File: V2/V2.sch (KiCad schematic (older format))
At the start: 184 parts, among them U1 Elite-C

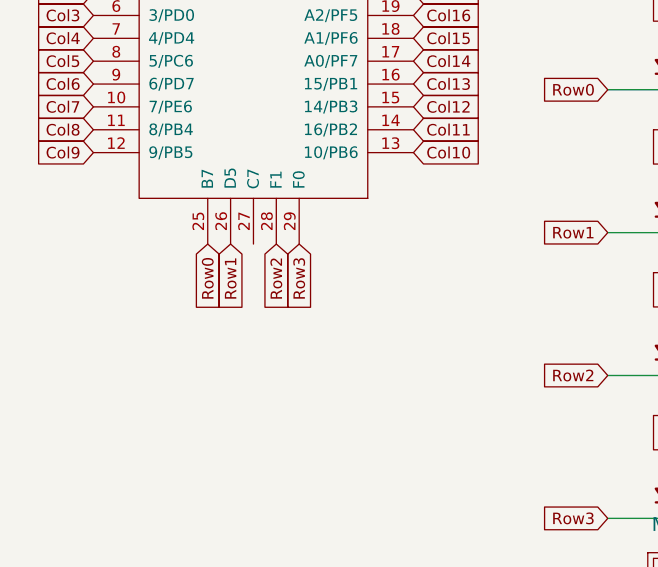
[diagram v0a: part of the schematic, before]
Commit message: Switched to LED
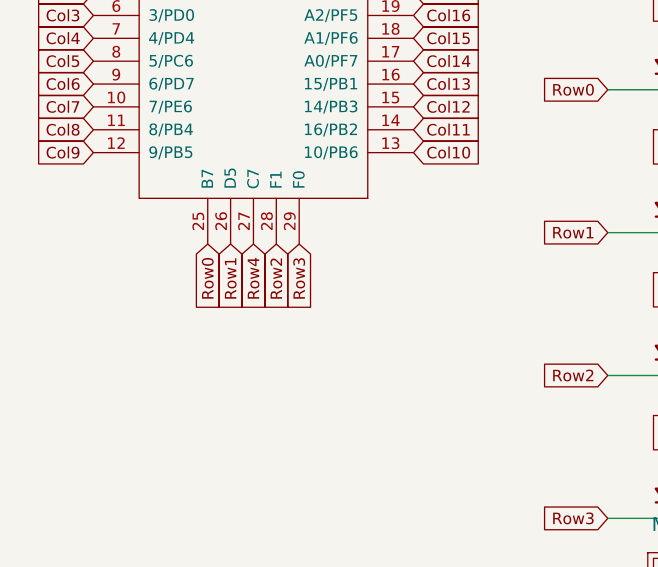
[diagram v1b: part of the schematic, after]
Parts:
- MX1, MX10, MX11, MX12, MX13, MX14, MX15, MX16, MX2, MX20, MX25, MX26, MX27, MX28, MX29, MX3, MX30, MX31, MX32, MX33, MX35, MX36, MX37, MX38, MX39, MX4, MX40, MX41, MX42, MX44, MX45, MX46, MX47, MX48, MX49, MX5, MX50, MX51, MX52, MX53, MX54, MX55, MX56, MX58, MX59, MX6, MX60, MX61, MX63, MX64, MX65, MX66, MX68, MX69, MX7, MX70, MX72, MX73, MX74, MX75, MX77, MX78, MX79, MX8, MX81, MX85, MX86, MX87, MX88, MX89, MX9, MX90, MX91: footprint MX_Alps_Hybrid:MXOnly-1U-Hotswap -> MX_Alps_Hybrid:MXOnly-1U
- MX17, MX18, MX82: footprint MX_Alps_Hybrid:MXOnly-2U-Hotswap -> MX_Alps_Hybrid:MXOnly-2U
- MX19, MX24, MX34, MX62, MX67, MX71, MX76: footprint MX_Alps_Hybrid:MXOnly-1.25U-Hotswap -> MX_Alps_Hybrid:MXOnly-1.25U
- MX21, MX83: footprint MX_Alps_Hybrid:MXOnly-1.5U-Hotswap -> MX_Alps_Hybrid:MXOnly-1.5U
- MX22, MX80: footprint MX_Alps_Hybrid:MXOnly-1.75U-Hotswap -> MX_Alps_Hybrid:MXOnly-1.75U
- MX23, MX84: footprint MX_Alps_Hybrid:MXOnly-2.25U-Hotswap -> MX_Alps_Hybrid:MXOnly-2.25U
- MX43: footprint MX_Alps_Hybrid:MXOnly-2.25U-Hotswap-ReversedStabilizers -> MX_Alps_Hybrid:MXOnly-2.25U-ReversedStabilizers
- MX57: footprint MX_Alps_Hybrid:MXOnly-2.75U-Hotswap-ReversedStabilizers -> MX_Alps_Hybrid:MXOnly-2.75U
- MX92: footprint MX_Alps_Hybrid:MXOnly-2U-Hotswap-ReversedStabilizers -> MX_Alps_Hybrid:MXOnly-2U-ReversedStabilizers
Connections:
- net Row4: now also U1.27 (C7)

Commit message: Update PCB
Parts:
- MX1, MX10, MX11, MX12, MX13, MX14, MX15, MX16, MX2, MX20, MX25, MX26, MX27, MX28, MX29, MX3, MX30, MX31, MX32, MX33, MX35, MX36, MX37, MX38, MX39, MX4, MX40, MX41, MX42, MX44, MX45, MX46, MX47, MX48, MX49, MX5, MX50, MX51, MX52, MX53, MX54, MX55, MX56, MX58, MX59, MX6, MX60, MX61, MX63, MX64, MX65, MX66, MX68, MX69, MX7, MX70, MX72, MX73, MX74, MX75, MX77, MX78, MX79, MX8, MX81, MX85, MX86, MX87, MX88, MX89, MX9, MX90, MX91: footprint MX_Alps_Hybrid:MXOnly-1U -> MX_Alps_Hybrid:MXOnly-1U-NoLED
- MX17, MX18: footprint MX_Alps_Hybrid:MXOnly-2U -> MX_Alps_Hybrid:MXOnly-2U-NoLED
- MX19, MX24, MX34, MX62, MX67, MX71, MX76: footprint MX_Alps_Hybrid:MXOnly-1.25U -> MX_Alps_Hybrid:MXOnly-1.25U-NoLED
- MX21, MX83: footprint MX_Alps_Hybrid:MXOnly-1.5U -> MX_Alps_Hybrid:MXOnly-1.5U-NoLED
- MX22, MX80: footprint MX_Alps_Hybrid:MXOnly-1.75U -> MX_Alps_Hybrid:MXOnly-1.75U-NoLED
- MX23, MX84: footprint MX_Alps_Hybrid:MXOnly-2.25U -> MX_Alps_Hybrid:MXOnly-2.25U-NoLED
- MX43: footprint MX_Alps_Hybrid:MXOnly-2.25U-ReversedStabilizers -> MX_Alps_Hybrid:MXOnly-2.25U-ReversedStabilizers-NoLED
- MX57: footprint MX_Alps_Hybrid:MXOnly-2.75U -> MX_Alps_Hybrid:MXOnly-2.75U-ReversedStabilizers-NoLED
- MX82: footprint MX_Alps_Hybrid:MXOnly-2U -> MX_Alps_Hybrid:MXOnly-2U-ReversedStabilizers-NoLED
- MX92: footprint MX_Alps_Hybrid:MXOnly-2U-ReversedStabilizers -> MX_Alps_Hybrid:MXOnly-2U-ReversedStabilizers-NoLED
